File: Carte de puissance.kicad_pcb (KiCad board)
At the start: 2 copper layers, 84 parts, among them J3 Pi_pwr, J4 Pi_data, J5 BAU1, J6 BAU2, J7 BAU3, J8 BAU4, J9 Programming, Q1 GSFP6901, Q2 GSFP6901, Q3 BC847, Q4 BC847, Q6 BC847, Q7 GSFP6901, Q8 BC847, SW1 SW_Push, SW2 Emergency switch (NC), U1 WeAct TPS5450 buck stepdown (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, U10 DPC817-B, U11 DPC817-B, U12 DPC817-B, U13 ATtiny1626-X, U2 WeAct TPS5450 buck stepdown (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, U3 WeAct TPS5450 buck stepdown (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, U5 PAC1811, U6 H11L1, U7 DPC817-B, U8 DPC817-B, U9 DPC817-B

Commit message: Placement pour avoir une carte au format du module
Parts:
- added F1: Fuse 9A, Fuse_custom:CONN_3557-2_KEY, F.Cu at (48.1, 110.1)
- added F2: Fuse 9A, Fuse_custom:CONN_3557-2_KEY, F.Cu at (63.1, 97.8)
- added F3: Fuse 9A, Fuse_custom:CONN_3557-2_KEY, F.Cu at (61.6, 85.0)
- added F4: Fuse 20A, Fuse_custom:CONN_3557-2_KEY, F.Cu at (54.5, 45.6)
- added F5: Fuse 9A, Fuse_custom:CONN_3557-2_KEY, F.Cu at (64.8, 44.0)
- added H1: MountingHole, MountingHole:MountingHole_3.2mm_M3, F.Cu at (41.0, 31.5)
- added H2: MountingHole, MountingHole:MountingHole_3.2mm_M3, F.Cu at (107.0, 31.5)
- added H3: MountingHole, MountingHole:MountingHole_3.2mm_M3, F.Cu at (107.0, 112.5)
- added H4: MountingHole, MountingHole:MountingHole_3.2mm_M3, F.Cu at (41.0, 112.5)
- C11, C12, C13, C14, C5, C7, C8, C9, D1, D2, D3, D4, D5, D6, D7, Q1, Q2, Q3, Q4, Q6, Q7, Q8, R1, R10, R11, R12, R13, R14, R15, R16, R17, R18, R19, R2, R20, R21, R22, R23, R24, R25, R26, R3, R4, R5, R6, R7, R8, R9, U10, U11, U12, U13, U5, U6, U7, U8, U9: moved to B.Cu
- moved BT1 143.4 mm to (53.1, 35.2)
- moved Q3 134.8 mm to (74.5, 43.7), turned to 90 degrees
- moved Q1 132.7 mm to (69.9, 45.7), turned to -90 degrees
- moved Q4 132.5 mm to (75.2, 51.4), turned to 180 degrees
- moved Q2 132.3 mm to (69.8, 53.2), turned to 90 degrees
- moved J9 125.9 mm to (69.3, 105.2), turned to -90 degrees
- moved Q7 123.2 mm to (80.0, 61.0), turned to -90 degrees
- moved D3 123.0 mm to (77.5, 43.2), turned to 90 degrees
- moved Q6 120.8 mm to (86.3, 60.2), turned to 90 degrees
- moved R21 119.6 mm to (74.8, 58.2)
- moved R22 119.2 mm to (75.5, 61.0), turned to -90 degrees
- moved R5 119.1 mm to (65.8, 53.5), turned to 90 degrees
- moved D1 118.4 mm to (69.3, 40.7)
- moved D4 117.1 mm to (68.2, 59.5), turned to -90 degrees
- moved D2 116.4 mm to (80.0, 46.2), turned to -90 degrees
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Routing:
- net LED_R: track 0.00 -> 33.4 mm
- net LED_G: track 0.00 -> 33.1 mm
- net LED_B: track 0.00 -> 33.0 mm
- added copper zone on In1.Cu, net GND
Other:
- board outline added: 73 x 88 mm
- copper layers 2 -> 4
- board text added: "Emplacement J1 (Vbatt, V_5v)"

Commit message: début de routage
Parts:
- U13: footprint Package_DFN_QFN:VQFN-20-1EP_3x3mm_P0.4mm_EP1.7x1.7mm -> Package_SO:SSOP-20_5.3x7.2mm_P0.65mm
- moved U13 17.8 mm to (92.3, 80.9), turned to -90 degrees
- moved C8 10.3 mm to (75.0, 65.0), turned to 90 degrees
- moved C14 9.73 mm to (87.0, 80.7), turned to -90 degrees
- moved D8 7.70 mm to (106.0, 89.9), turned to 90 degrees
- moved Q8 3.99 mm to (92.4, 92.1)
- moved R23 2.96 mm to (91.0, 89.2)
- moved R24 1.79 mm to (95.2, 91.2), turned to 90 degrees
- moved R20 1.12 mm to (96.0, 95.2), turned to -135 degrees
- moved C13 0.93 mm to (72.4, 72.6), turned to -90 degrees
- moved D7 0.75 mm to (79.8, 66.5)
- moved R15 0.73 mm to (87.8, 55.1)
- moved R12 0.51 mm to (91.8, 65.7)
- moved R11 0.28 mm to (82.0, 50.8), turned to 90 degrees
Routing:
- net VCC: track 0.00 -> 92.5 mm
- net EN_BATT: track 0.00 -> 40.4 mm, vias 0 -> 2
- net BAU_IN: track 0.00 -> 40.3 mm
- net PWR_BTN: track 0.00 -> 38.5 mm, vias 0 -> 2
- net EN_PI: track 0.00 -> 34.4 mm
- net BATT_SENSE: track 0.00 -> 34.2 mm
- net UPDI: track 0.00 -> 32.8 mm
- net SCL: track 0.00 -> 29.3 mm
- net LED_B: track 33.0 -> 15.4 mm
- net BAU_EXT: track 0.00 -> 16.6 mm
- net LED_G: track 33.1 -> 17.0 mm
- net Net-(Q8-C): track 0.00 -> 15.8 mm
- net BAU_OUT: track 0.00 -> 15.5 mm, vias 0 -> 1
- net EN_EXTPWR: track 0.00 -> 15.2 mm
- net LED_R: track 33.4 -> 18.7 mm
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- added copper zone on F.Cu, net +BATT
- added copper zone on In2.Cu, net +V_PI
- added copper zone on In2.Cu, net Net-(ALM1-Pin_3)
- added copper zone on In2.Cu, net Net-(ALM4-Pin_3)
- added copper zone on B.Cu, net Net-(D1-A)
- added copper zone on B.Cu, net Net-(D1-K)
- added copper zone on B.Cu, net Net-(D3-A)
- added copper zone on B.Cu, net Net-(D6-A)
- added copper zone on B.Cu, net Net-(Q1-Pad5)
- added copper zone on B.Cu, net Net-(Q3-B)
- added copper zone on B.Cu, net Net-(Q6-B)
- added copper zone on B.Cu, net VCC
- added copper zone on B.Cu, net VSENSE+
- added copper zone on B.Cu, net VSENSE-

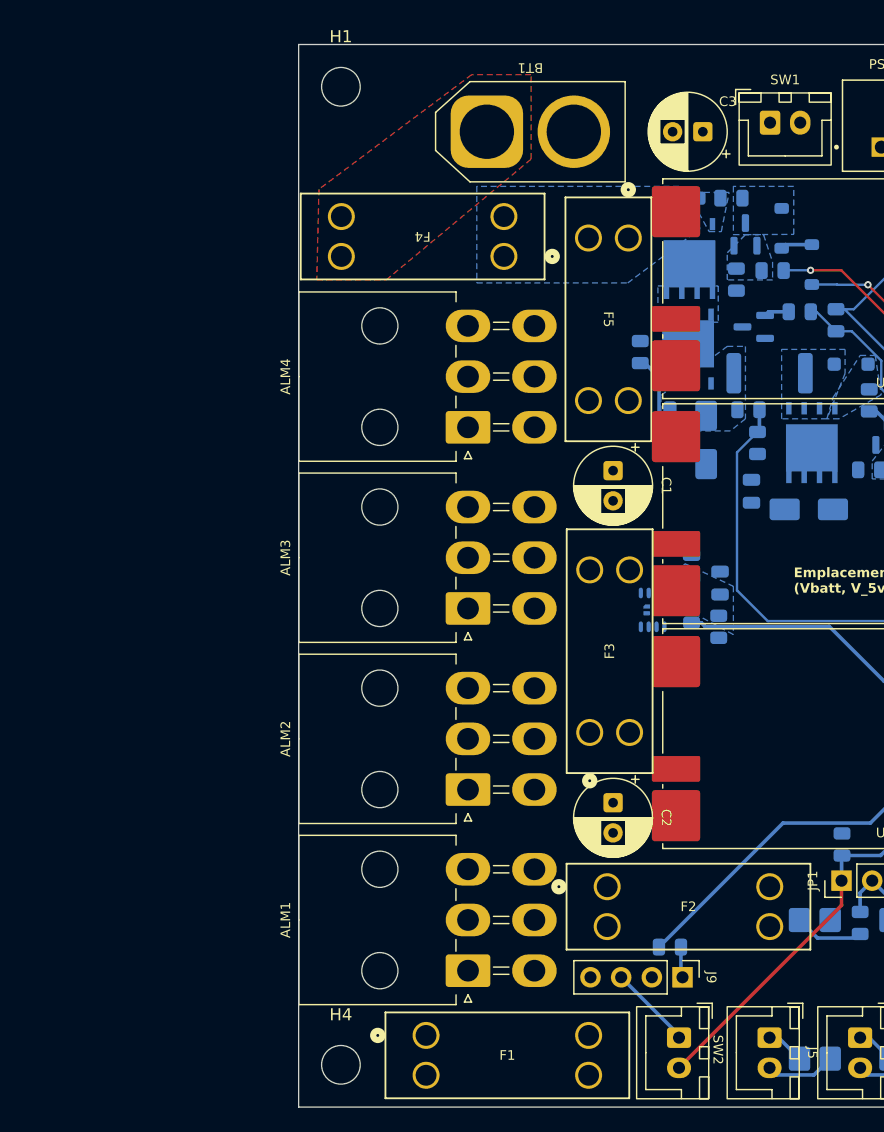
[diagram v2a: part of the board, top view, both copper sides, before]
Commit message: Changement des empreintes de fusible
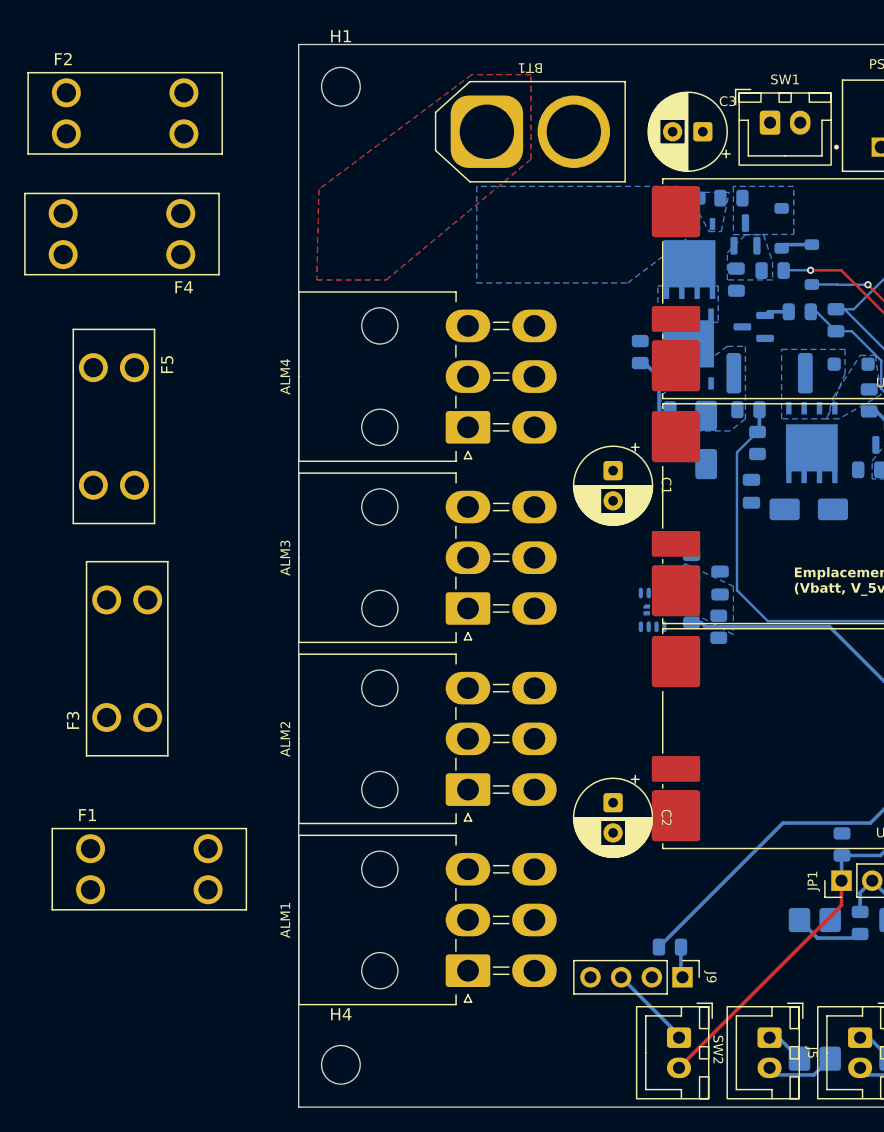
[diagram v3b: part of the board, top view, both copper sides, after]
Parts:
- F1, F2, F3, F4, F5: footprint Fuse_custom:CONN_3557-2_KEY -> 3557-2_fuseholder:FUSE_3557_simple
- moved F2 74.5 mm to (25.0, 33.7)
- moved F5 46.0 mm to (22.2, 61.5)
- moved F3 39.1 mm to (23.3, 77.0)
- moved F4 33.5 mm to (21.0, 43.7)
- moved F1 25.2 mm to (27.0, 96.3)

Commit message: Ajout de l'empreinte des MR30PB
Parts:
- added J1: 5v external regulator, MR30PB:MR30PB, F.Cu at (128.0, 67.5)
- added J2: other external regulator, MR30PB:MR30PB, F.Cu at (128.0, 74.4)

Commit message: Routage V2 partiel
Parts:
- ALM1, ALM2, ALM3, ALM4: footprint Connector_Molex:Molex_Mini-Fit_Jr_5569-06A2_2x03_P4.20mm_Horizontal -> Molex:Molex_Mini-Fit_Jr_5569-06A2_2x03_P4.20mm_Horizontal
- C11, C12, C13, C14, C5, C7, C8, C9, D1, D2, D3, D4, D5, D6, D7, Q1, Q2, Q3, Q4, Q6, Q7, Q8, R1, R10, R11, R12, R13, R14, R15, R16, R17, R18, R19, R2, R20, R21, R22, R23, R24, R25, R26, R3, R4, R5, R6, R7, R8, R9, U13, U5: moved to F.Cu
- moved R26 154.3 mm to (222.5, 98.4), turned to 0 degrees
- moved R25 140.0 mm to (222.5, 95.5), turned to 0 degrees
- moved R6 140.0 mm to (209.2, 101.4), turned to 0 degrees
- moved R11 139.0 mm to (213.7, 95.5), turned to 0 degrees
- moved R15 136.2 mm to (213.7, 107.3), turned to 0 degrees
- moved C8 134.9 mm to (209.8, 58.9), turned to 180 degrees
- moved R23 131.5 mm to (222.5, 89.6), turned to 0 degrees
- moved R24 127.2 mm to (222.5, 92.5), turned to 0 degrees
- moved F2 126.3 mm to (124.1, 112.0), turned to 180 degrees
- moved R12 126.2 mm to (213.7, 98.4), turned to 0 degrees
- moved Q4 120.9 mm to (191.5, 84.6), turned to 0 degrees
- moved R16 120.1 mm to (218.1, 89.6), turned to 0 degrees
- moved JP1 119.9 mm to (187.6, 39.8), turned to 0 degrees
- moved R13 117.1 mm to (213.7, 101.4), turned to 0 degrees
- moved C13 117.1 mm to (186.8, 97.5), turned to 0 degrees
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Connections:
- net VSENSE- renamed +VSW
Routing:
- net +V_BATT: track 0.00 -> 118.7 mm, vias 0 -> 15
- net VCC: track 92.5 -> 2.34 mm, vias 0 -> 1
- net EN_BATT: track 40.4 -> 0.00 mm, vias 2 -> 0
- net BAU_IN: track 40.3 -> 0.00 mm
- net PWR_BTN: track 38.5 -> 0.00 mm, vias 2 -> 0
- net EN_PI: track 34.4 -> 0.00 mm
- net UPDI: track 32.8 -> 0.00 mm
- net BATT_SENSE: track 34.2 -> 2.25 mm
- net SCL: track 29.3 -> 0.00 mm
- net LED_R: track 18.7 -> 0.00 mm
- net Net-(J5-Pin_2): track 5.82 -> 24.2 mm
- net LED_G: track 17.0 -> 0.00 mm
- net +VSW: track 0.00 -> 16.8 mm, vias 0 -> 14
- net BAU_EXT: track 16.6 -> 0.00 mm
- net Net-(Q8-C): track 15.8 -> 0.00 mm
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- added copper zone on B.Cu, net +BATT
- added copper zone on F.Cu, net +VSW
- added copper zone on B.Cu, net +V_BATT
- added copper zone on F.Cu, net +V_BATT
- added copper zone on F.Cu, net GND
- added copper zone on F.Cu, net Net-(D1-K)
- added copper zone on F.Cu, net Net-(Q1-Pad5)
- added copper zone on F.Cu, net VSENSE+
- removed copper zone on In2.Cu, net +V_PI
- removed copper zone on In2.Cu, net Net-(ALM1-Pin_3)
- removed copper zone on In2.Cu, net Net-(ALM4-Pin_3)
- removed copper zone on B.Cu, net Net-(D1-A)
- removed copper zone on B.Cu, net Net-(D3-A)
- removed copper zone on B.Cu, net Net-(D6-A)
- removed copper zone on B.Cu, net Net-(Q3-B)
- removed copper zone on B.Cu, net Net-(Q6-B)
- removed copper zone on B.Cu, net VCC
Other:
- board size 73 x 88 mm -> 73 x 98 mm
- board text removed: "Emplacement J1 (Vbatt, V_5v)"

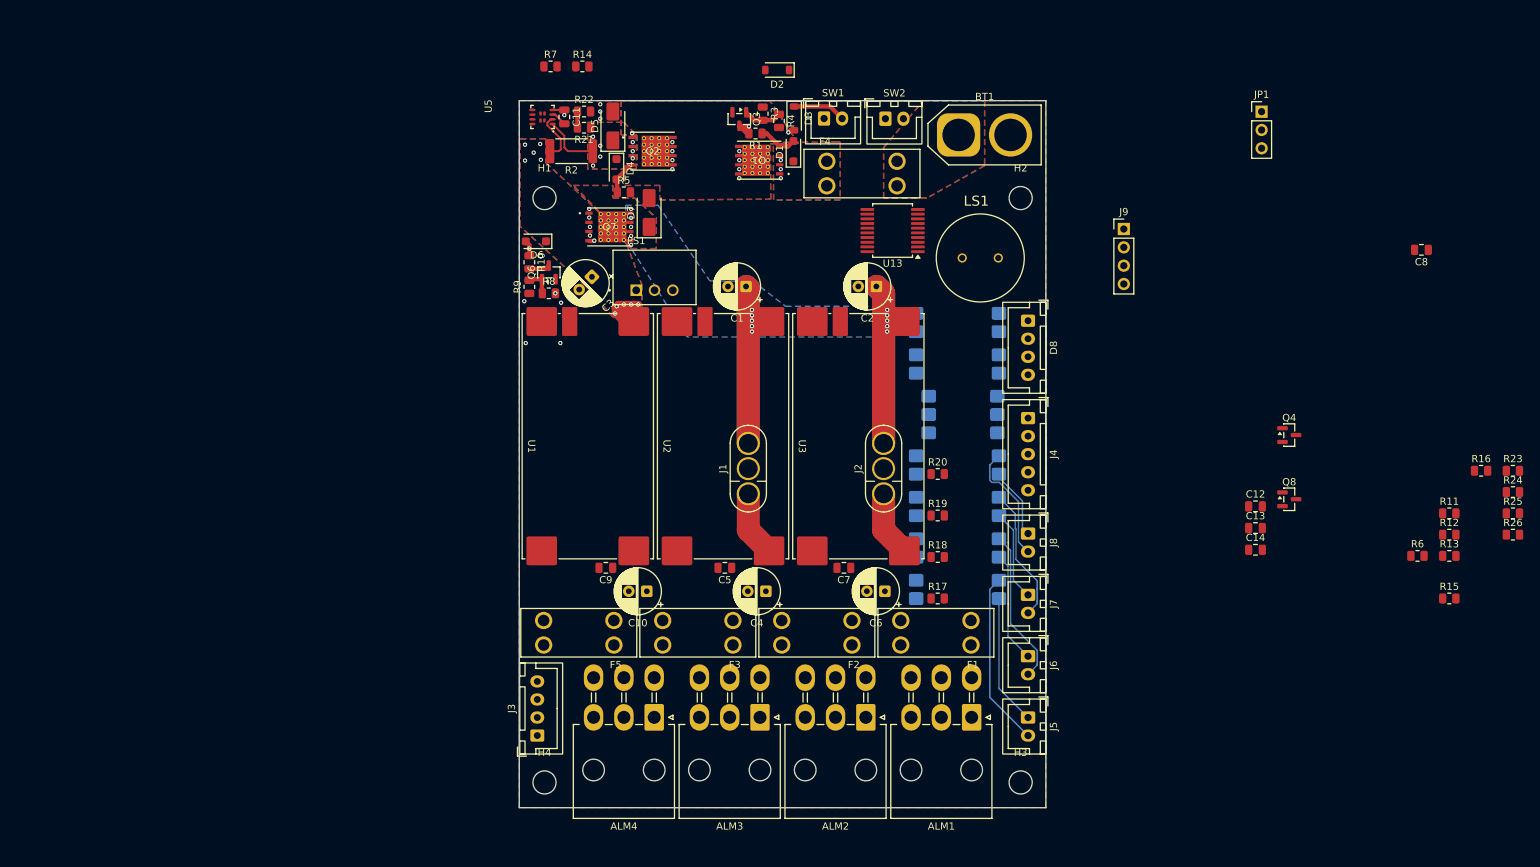
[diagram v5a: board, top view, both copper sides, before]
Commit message: Routage V2 signaux fini Il reste encore la puissance à finir
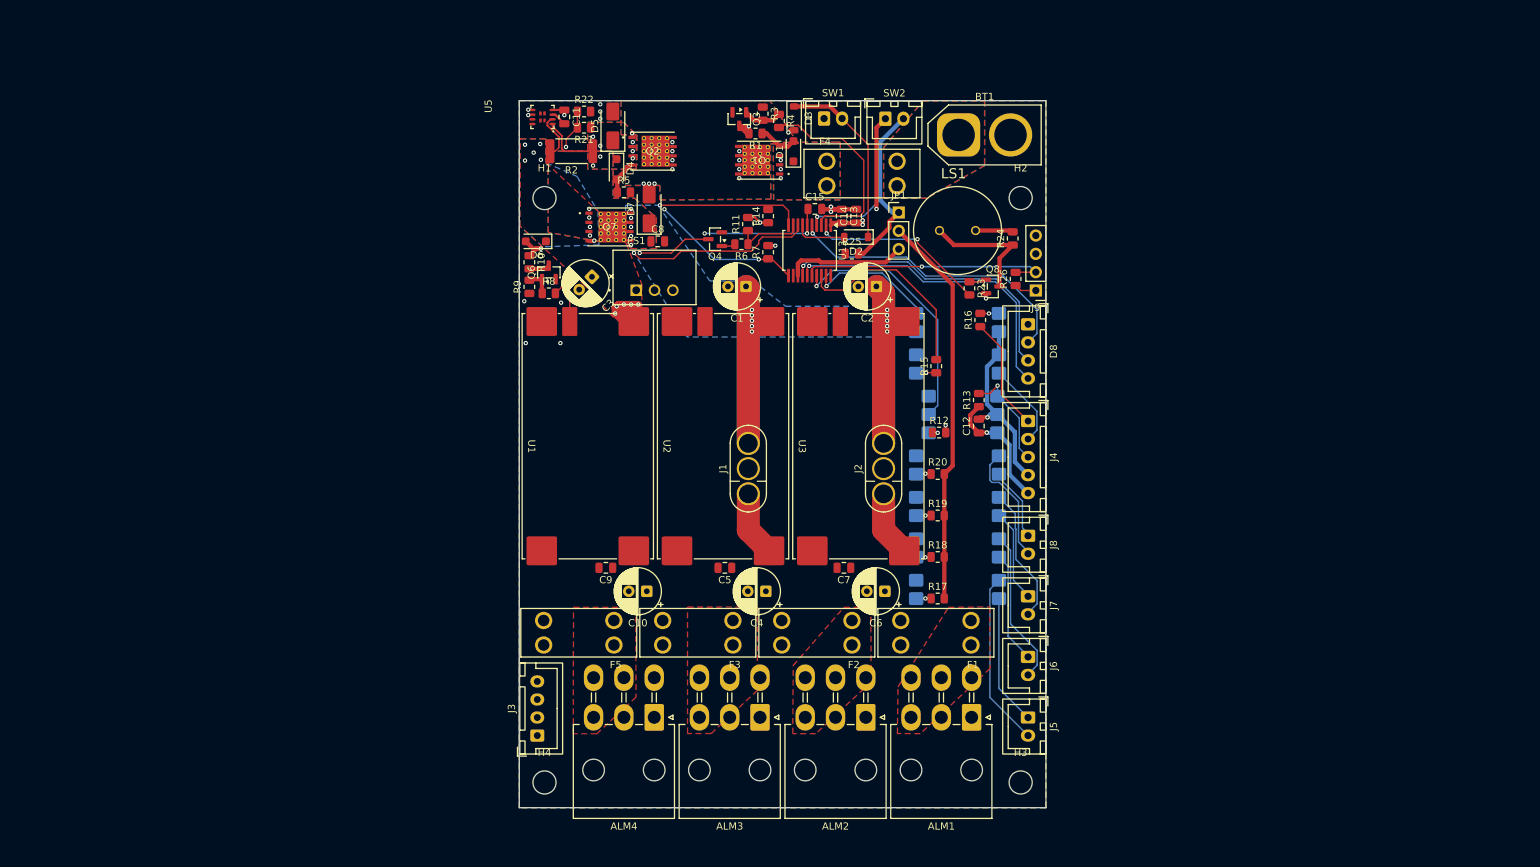
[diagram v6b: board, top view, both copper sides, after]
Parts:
- added C15: 100nF, Capacitor_SMD:C_0805_2012Metric, F.Cu at (125.7, 53.3)
- moved C8 105.9 mm to (103.9, 57.8), turned to 0 degrees
- moved R11 105.2 mm to (116.4, 55.4), turned to 90 degrees
- moved R6 103.2 mm to (115.5, 58.2), turned to 180 degrees
- moved R25 98.5 mm to (130.8, 59.5)
- moved Q4 84.1 mm to (111.9, 57.5), turned to 180 degrees
- moved R23 79.5 mm to (147.1, 64.3), turned to -90 degrees
- moved R15 78.1 mm to (142.5, 75.1), turned to 90 degrees
- moved R24 77.7 mm to (153.1, 57.4), turned to 90 degrees
- moved R26 77.5 mm to (153.5, 63.0), turned to 90 degrees
- moved R16 72.5 mm to (148.6, 68.7), turned to 90 degrees
- moved C14 72.1 mm to (131.4, 54.3), turned to 90 degrees
- moved R12 72.1 mm to (142.9, 84.3)
- moved C13 71.8 mm to (129.4, 54.3), turned to -90 degrees
- moved R13 68.7 mm to (148.4, 79.8), turned to 90 degrees
- moved JP1 52.2 mm to (137.3, 53.8)
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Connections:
- U13 pad 14: BAU_IN -> LED_G
- U13 pad 15: BUZZER -> LED_B
- U13 pad 2: BATT_SENSE -> BUZZER
- U13 pad 4: PWR_BTN -> BAU_IN
- U13 pad 6: LED_G -> BATT_SENSE
- U13 pad 7: LED_B -> PWR_BTN
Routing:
- net VCC: track 2.34 -> 58.5 mm, vias 1 -> 7
- net BAU_EXT: track 0.00 -> 54.5 mm
- net SCL: track 0.00 -> 49.5 mm, vias 0 -> 3
- net BATT_SENSE: track 2.25 -> 50.5 mm, vias 0 -> 3
- net SDA: track 0.00 -> 46.9 mm, vias 0 -> 2
- net LED_B: track 0.00 -> 43.5 mm, vias 0 -> 1
- net LED_G: track 0.00 -> 42.6 mm, vias 0 -> 1
- net LED_R: track 0.00 -> 41.7 mm, vias 0 -> 1
- net EN_EXTPWR: track 0.00 -> 39.2 mm, vias 1 -> 2
- net TX: track 0.00 -> 35.6 mm, vias 0 -> 1
- net UPDI: track 0.00 -> 35.2 mm, vias 0 -> 1
- net BAU_IN: track 0.00 -> 35.2 mm, vias 0 -> 1
- net EN_BATT: track 0.00 -> 28.2 mm
- net SHUTDOWN_PI: track 0.00 -> 28.0 mm
- net Net-(Q4-C): track 0.00 -> 27.1 mm, vias 0 -> 2
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- added copper zone on B.Cu, net GND
- added copper zone on In2.Cu, net GND
- added copper zone on F.Cu, net Net-(ALM1-Pin_3)
- added copper zone on F.Cu, net Net-(ALM2-Pin_3)
- added copper zone on F.Cu, net Net-(ALM3-Pin_3)
- added copper zone on F.Cu, net Net-(ALM4-Pin_3)
- added copper zone on In2.Cu, net VCC

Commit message: Routage fini reste à corriger les erreurs DRC, et à faire les graphiques
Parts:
- moved C5 9.43 mm to (122.6, 103.8), turned to 0 degrees
- moved C7 9.10 mm to (138.7, 104.4), turned to -90 degrees
- moved C6 1.72 mm to (134.2, 105.0), turned to -90 degrees
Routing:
- net +V_other: track 9.09 -> 99.1 mm, vias 0 -> 16
- net +V_5v: track 9.09 -> 92.6 mm, vias 0 -> 4
- net +V_PI: track 0.00 -> 43.0 mm, vias 0 -> 3
- net Net-(R17-Pad1): track 2.09 -> 4.11 mm
- net +V_BATT: vias 15 -> 21
- added copper zone on In2.Cu, net +V_5v
- added copper zone on In2.Cu, net +V_BATT
- added copper zone on B.Cu, net +V_other
- added copper zone on B.Cu, net Net-(ALM1-Pin_3)
- added copper zone on B.Cu, net Net-(ALM2-Pin_3)
- added copper zone on B.Cu, net Net-(ALM3-Pin_3)
- added copper zone on B.Cu, net Net-(ALM4-Pin_3)
